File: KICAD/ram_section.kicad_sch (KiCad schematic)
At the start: 6 parts

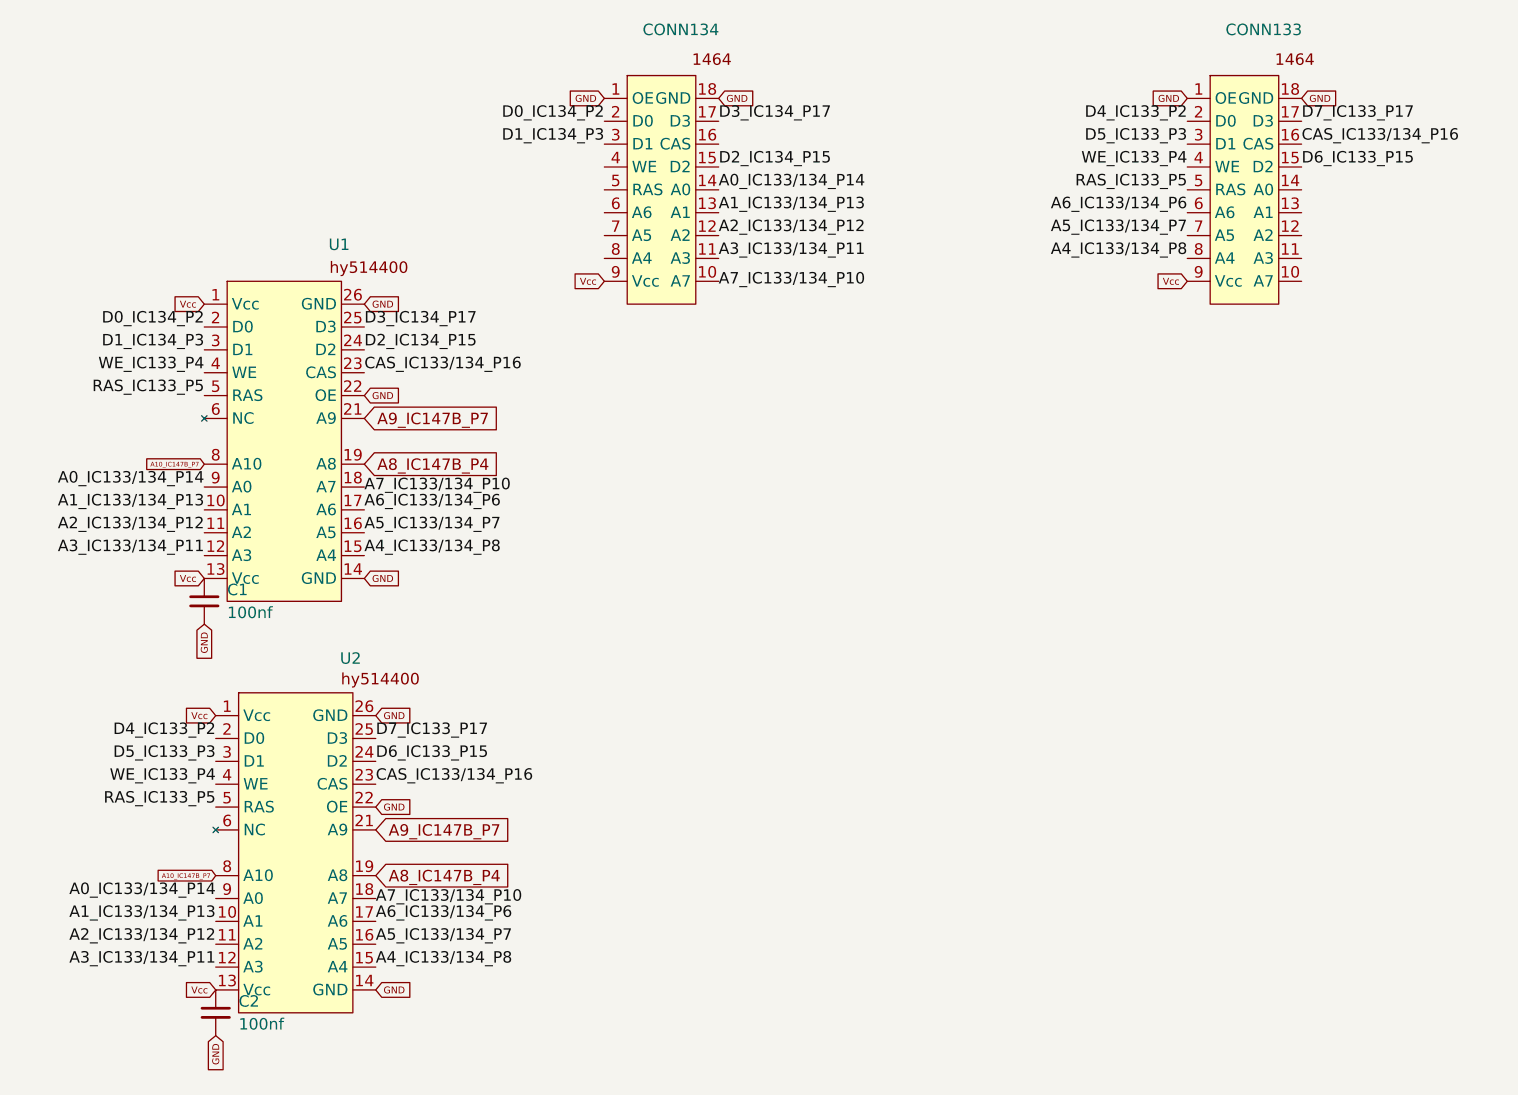
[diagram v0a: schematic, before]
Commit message: Update component values and BOM
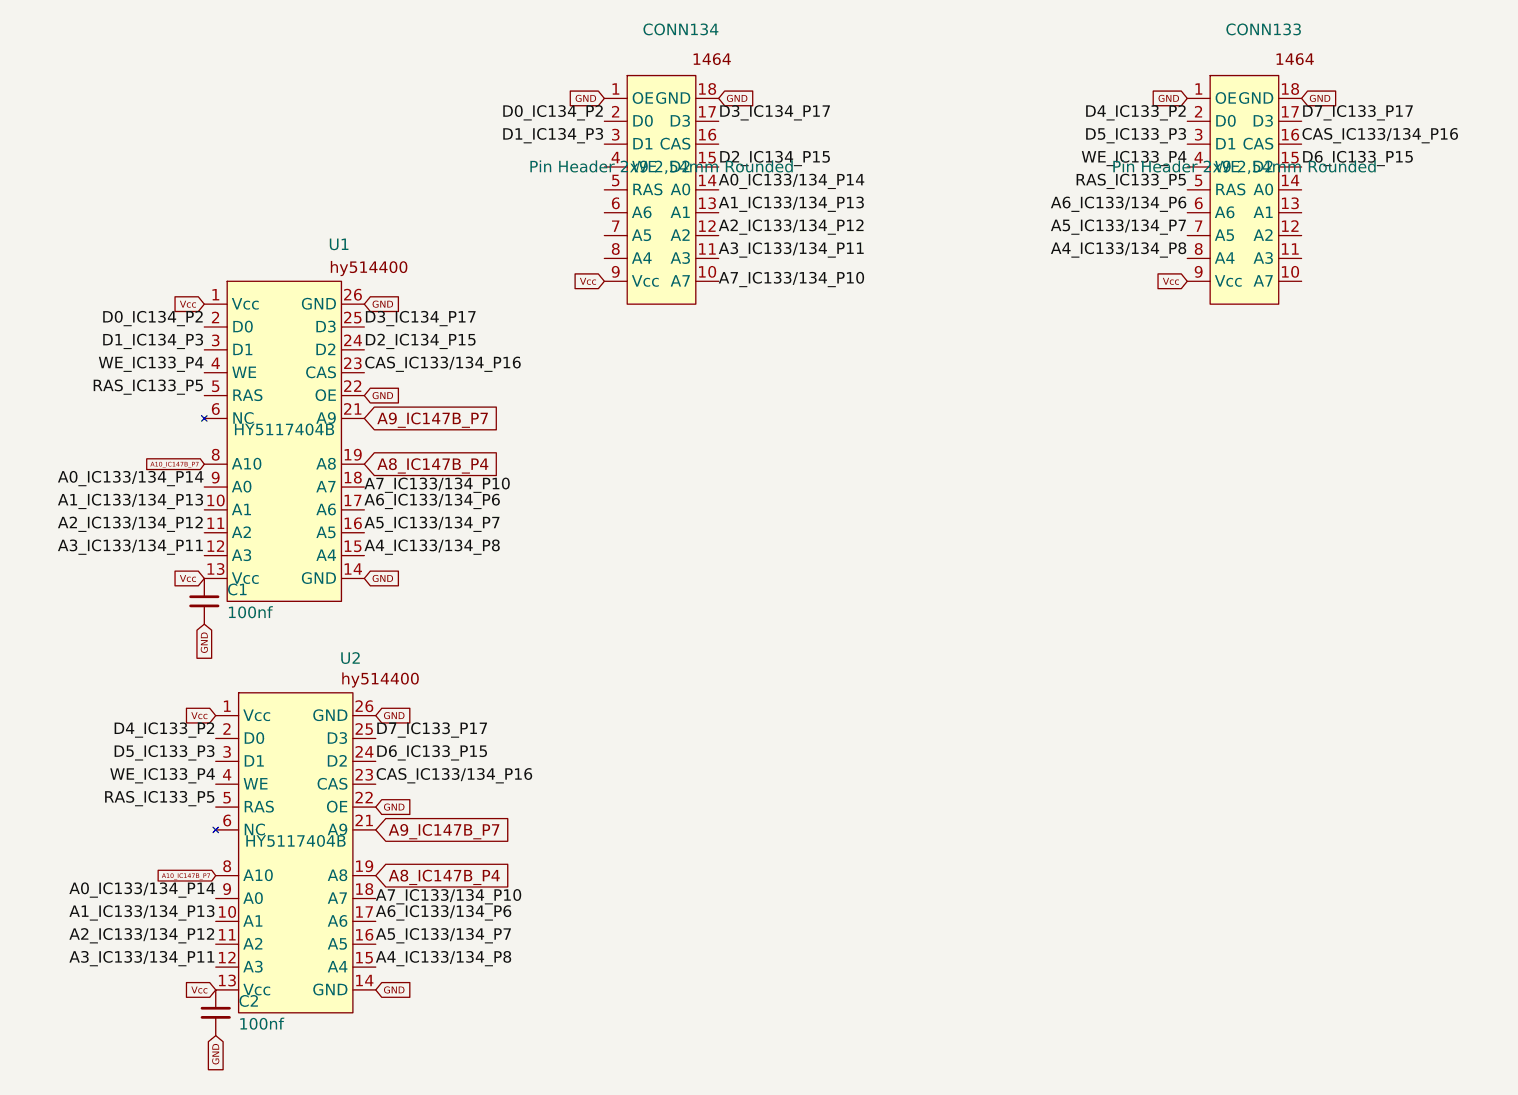
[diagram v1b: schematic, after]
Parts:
- CONN133, CONN134: value (none) -> Pin Header 2x9 2,54mm Rounded
- U1, U2: value (none) -> HY5117404B
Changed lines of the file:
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@@
 			)
 		)
-		(property "Value" ""
+		(property "Value" "HY5117404B"
 			(at 78.74 128.27 0)
 			(show_name no)
@@
 			)
 		)
-		(property "Value" ""
+		(property "Value" "Pin Header 2x9 2,54mm Rounded"
 			(at 184.15 53.34 0)
 			(show_name no)
@@
 			)
 		)
-		(property "Value" ""
+		(property "Value" "Pin Header 2x9 2,54mm Rounded"
 			(at 119.38 53.34 0)
 			(show_name no)
@@
 			)
 		)
-		(property "Value" ""
+		(property "Value" "HY5117404B"
 			(at 77.47 82.55 0)
 			(show_name no)
